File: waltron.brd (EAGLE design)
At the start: 53.6 x 45.1 mm, 25 parts, among them IC1 4049N, U1 LM386

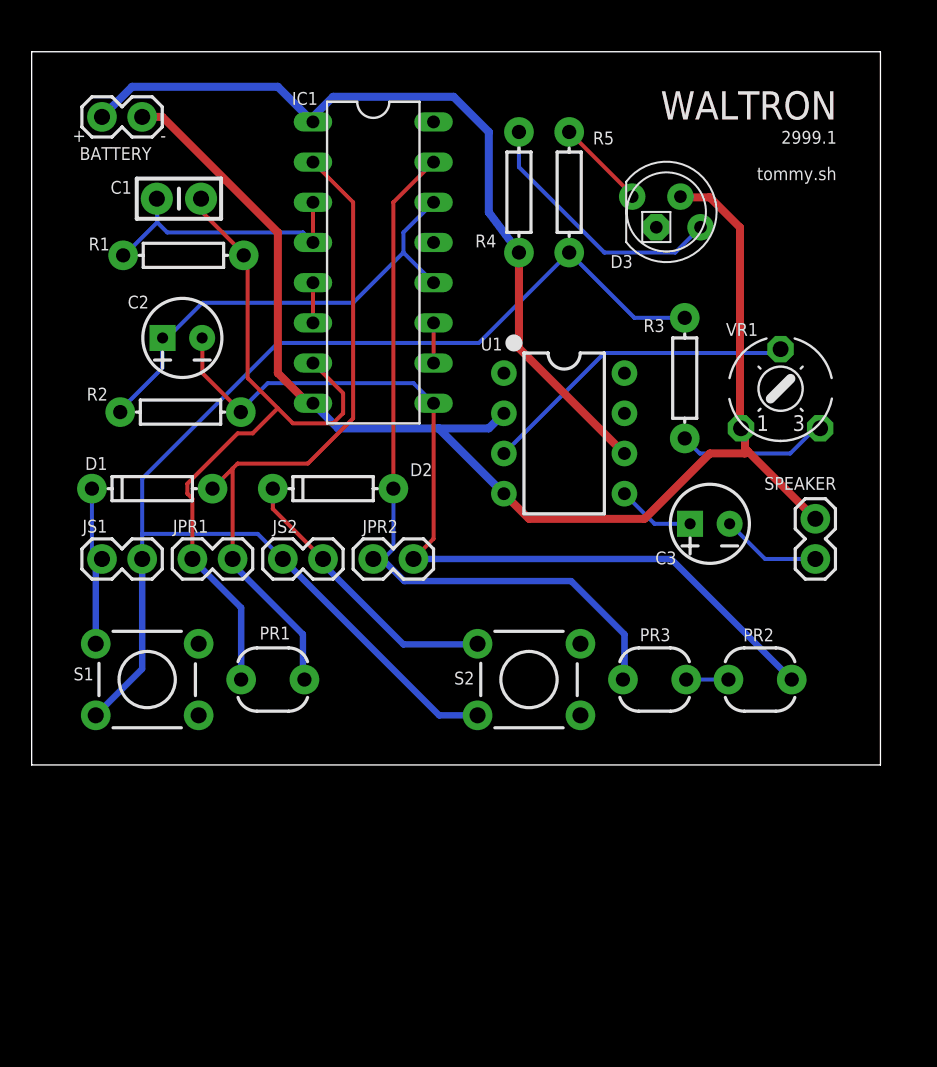
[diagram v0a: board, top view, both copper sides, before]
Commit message: Update schematic w/ 2999.1 concerns
- use IC name for LM386 instead of U1
- switch trim pot to model used in 4step
- add switch connection
- consistent J names for speaker and battery
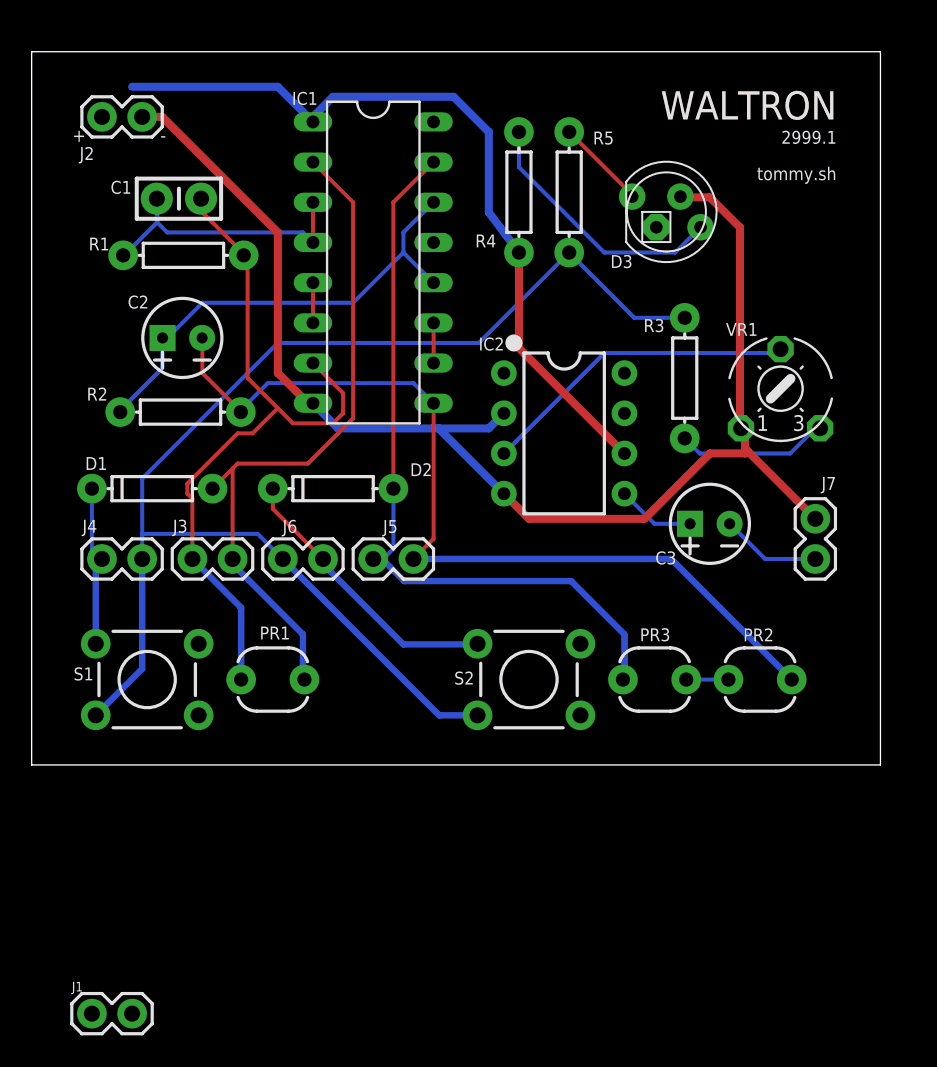
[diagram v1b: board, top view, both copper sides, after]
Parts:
- added J1: On Switch, SparkFun-Connectors:1X02
- J2: value 9v -> 9v battery
- J7: value 8ohm -> 8ohm speaker
- renumbered BATTERY to J2, JPR1 to J3, JPR2 to J5, JS1 to J4, JS2 to J6, SPEAKER to J7, U1 to IC2
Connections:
- new net N$19: J1.2, J2.1
- net V+: now also J1.1; no longer J2.1
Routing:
- net V+: track 51.6 -> 48.9 mm
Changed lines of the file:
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@@
 <attribute name="VALUE" x="31.4325" y="2.2225" size="0.6096" layer="27" font="vector" ratio="20" align="top-center"/>
 </element>
-<element name="U1" library="SparkFun-IC-Amplifiers" package="DIP08" value="LM386" x="33.655" y="20.955" smashed="yes" rot="R270">
+<element name="IC2" library="SparkFun-IC-Amplifiers" package="DIP08" value="LM386" x="33.655" y="20.955" smashed="yes" rot="R270">
 <attribute name="NAME" x="29.0631375" y="26.19375" size="0.8128" layer="25" font="vector" ratio="10" align="bottom-center"/>
 <attribute name="PROD_ID" value="IC-10899" x="33.655" y="20.955" size="1.778" layer="27" rot="R270" display="off"/>
 <attribute name="VALUE" x="33.654996875" y="23.6536125" size="0.8128" layer="27" font="vector" ratio="10" align="bottom-center"/>
 </element>
-<element name="BATTERY" library="SparkFun-Connectors" package="1X02" value="9v" x="4.445" y="40.9575" smashed="yes">
+<element name="J2" library="SparkFun-Connectors" package="1X02" value="9v battery" x="4.445" y="40.9575" smashed="yes">
 <attribute name="NAME" x="3.029021875" y="38.23300625" size="0.8128" layer="25" font="vector" ratio="10"/>
 </element>
-<element name="SPEAKER" library="SparkFun-Connectors" package="1X02" value="8ohm" x="49.53" y="13.0175" smashed="yes" rot="R90">
+<element name="J7" library="SparkFun-Connectors" package="1X02" value="8ohm speaker" x="49.53" y="13.0175" smashed="yes" rot="R90">
 <attribute name="NAME" x="50.85201875" y="18.20015" size="0.8128" layer="25" font="vector" ratio="10" rot="R180"/>
 </element>
@@
 <attribute name="NAME" x="45.90170625" y="27.92785" size="0.8128" layer="25" font="vector" ratio="10" rot="R180"/>
 </element>
-<element name="JPR1" library="SparkFun-Connectors" package="1X02" value="" x="10.16" y="13.0175" smashed="yes">
+<element name="J3" library="SparkFun-Connectors" package="1X02" value="" x="10.16" y="13.0175" smashed="yes">
 <attribute name="NAME" x="8.925678125" y="14.6828" size="0.8128" layer="25" font="vector" ratio="10"/>
 <attribute name="VALUE" x="8.89" y="10.9855" size="0.6096" layer="27" font="vector" ratio="20"/>
 </element>
-<element name="JS1" library="SparkFun-Connectors" package="1X02" value="" x="4.445" y="13.0175" smashed="yes">
+<element name="J4" library="SparkFun-Connectors" package="1X02" value="" x="4.445" y="13.0175" smashed="yes">
 <attribute name="NAME" x="3.210678125" y="14.6828" size="0.8128" layer="25" font="vector" ratio="10"/>
 <attribute name="VALUE" x="3.175" y="10.9855" size="0.6096" layer="27" font="vector" ratio="20"/>
 </element>
-<element name="JPR2" library="SparkFun-Connectors" package="1X02" value="" x="24.13" y="13.0175" smashed="yes" rot="R180">
+<element name="J5" library="SparkFun-Connectors" package="1X02" value="" x="24.13" y="13.0175" smashed="yes" rot="R180">
 <attribute name="NAME" x="23.141821875" y="15.4797" size="0.8128" layer="25" font="vector" ratio="10" rot="R180"/>
 <attribute name="VALUE" x="25.4" y="15.0495" size="0.6096" layer="27" font="vector" ratio="20" rot="R180"/>
 </element>
-<element name="JS2" library="SparkFun-Connectors" package="1X02" value="" x="18.415" y="13.0175" smashed="yes" rot="R180">
+<element name="J6" library="SparkFun-Connectors" package="1X02" value="" x="18.415" y="13.0175" smashed="yes" rot="R180">
 <attribute name="NAME" x="16.791821875" y="15.4797" size="0.8128" layer="25" font="vector" ratio="10" rot="R180"/>
 <attribute name="VALUE" x="19.685" y="15.0495" size="0.6096" layer="27" font="vector" ratio="20" rot="R180"/>
@@
 <attribute name="NAME" x="36.57574375" y="31.409234375" size="0.8128" layer="21" font="vector" ratio="10"/>
 </element>
+<element name="J1" library="SparkFun-Connectors" package="1X02" value="On Switch" x="3.81" y="-15.71625"/>
 </elements>
 <signals>
@@
 <contactref element="R1" pad="P$1"/>
 <contactref element="C1" pad="1"/>
-<contactref element="JPR1" pad="1"/>
+<contactref element="J3" pad="1"/>
 <wire x1="10.16" y1="13.0175" x2="13.24" y2="9.9375" width="0.4064" layer="16"/>
 <wire x1="13.24" y1="9.9375" x2="13.24" y2="5.3975" width="0.4064" layer="16"/>
@@
 <contactref element="IC1" pad="2"/>
 <contactref element="D1" pad="A"/>
-<contactref element="JPR1" pad="2"/>
+<contactref element="J3" pad="2"/>
 <wire x1="12.7" y1="13.0175" x2="12.7" y2="12.7" width="0.4064" layer="16"/>
 <wire x1="12.7" y1="12.7" x2="17.145" y2="8.255" width="0.4064" layer="16"/>
@@
 <contactref element="C2" pad="2"/>
 <contactref element="PR2" pad="1"/>
-<contactref element="JPR2" pad="1"/>
+<contactref element="J5" pad="1"/>
 <wire x1="24.13" y1="13.0175" x2="40.4175" y2="13.0175" width="0.4064" layer="16"/>
 <wire x1="40.4175" y1="13.0175" x2="48.0375" y2="5.3975" width="0.4064" layer="16"/>
@@
 <contactref element="PR3" pad="2"/>
 <contactref element="D2" pad="A"/>
-<contactref element="JPR2" pad="2"/>
+<contactref element="J5" pad="2"/>
 <wire x1="21.59" y1="13.0175" x2="22.1543375" y2="13.0175" width="0.4064" layer="16"/>
 <wire x1="22.1543375" y1="13.0175" x2="23.5513375" y2="11.6205" width="0.4064" layer="16"/>
@@
 <contactref element="R3" pad="P$1"/>
 <contactref element="R5" pad="P$1"/>
-<contactref element="JS1" pad="2"/>
-<contactref element="JS2" pad="2"/>
+<contactref element="J4" pad="2"/>
+<contactref element="J6" pad="2"/>
 <wire x1="15.875" y1="13.0175" x2="25.7556" y2="3.1369" width="0.4064" layer="16"/>
 <wire x1="25.7556" y1="3.1369" x2="28.1813" y2="3.1369" width="0.4064" layer="16"/>
@@
 </signal>
 <signal name="N$14">
-<contactref element="U1" pad="5"/>
+<contactref element="IC2" pad="5"/>
 <contactref element="C3" pad="1"/>
 <wire x1="39.37" y1="15.24" x2="37.465" y2="17.145" width="0.254" layer="16"/>
@@
 <signal name="N$15">
 <contactref element="C3" pad="2"/>
-<contactref element="SPEAKER" pad="1"/>
+<contactref element="J7" pad="1"/>
 <wire x1="46.355" y1="13.0175" x2="44.1325" y2="15.24" width="0.254" layer="16"/>
 <wire x1="49.53" y1="13.0175" x2="46.355" y2="13.0175" width="0.254" layer="16"/>
@@
 <contactref element="D1" pad="C"/>
 <contactref element="S1" pad="1"/>
-<contactref element="JS1" pad="1"/>
+<contactref element="J4" pad="1"/>
 <wire x1="4.445" y1="13.0175" x2="4.0513" y2="12.6238" width="0.4064" layer="16"/>
 <wire x1="4.0513" y1="12.6238" x2="4.0513" y2="7.6581" width="0.4064" layer="16"/>
@@
 <contactref element="D2" pad="C"/>
 <contactref element="S2" pad="1"/>
-<contactref element="JS2" pad="1"/>
+<contactref element="J6" pad="1"/>
 <wire x1="18.415" y1="13.0175" x2="18.415" y2="12.7" width="0.4064" layer="16"/>
 <wire x1="18.415" y1="12.7" x2="23.495" y2="7.62" width="0.4064" layer="16"/>
@@
 </signal>
 <signal name="V+" class="1">
-<contactref element="BATTERY" pad="1"/>
-<contactref element="U1" pad="6"/>
+<contactref element="IC2" pad="6"/>
 <contactref element="R4" pad="P$1"/>
 <contactref element="IC1" pad="1"/>
 <wire x1="15.5575" y1="42.8625" x2="17.78" y2="40.64" width="0.508" layer="16"/>
 <wire x1="6.35" y1="42.8625" x2="15.5575" y2="42.8625" width="0.508" layer="16"/>
-<wire x1="4.445" y1="40.9575" x2="6.35" y2="42.8625" width="0.508" layer="16"/>
 <wire x1="30.7975" y1="26.3525" x2="37.465" y2="19.685" width="0.508" layer="1"/>
 <wire x1="30.7975" y1="32.385" x2="30.7975" y2="26.3525" width="0.508" layer="1"/>
@@
 <wire x1="30.7975" y1="32.385" x2="28.8925" y2="34.925" width="0.508" layer="16"/>
 <wire x1="17.78" y1="40.64" x2="17.78" y2="40.9575" width="0.508" layer="16"/>
+<contactref element="J1" pad="1"/>
+<wire x1="3.81" y1="-15.71625" x2="37.465" y2="19.685" width="0" layer="19" extent="1-1"/>
 </signal>
 <signal name="GND" class="1">
-<contactref element="U1" pad="2"/>
-<contactref element="U1" pad="4"/>
-<contactref element="SPEAKER" pad="2"/>
-<contactref element="BATTERY" pad="2"/>
+<contactref element="IC2" pad="2"/>
+<contactref element="IC2" pad="4"/>
+<contactref element="J7" pad="2"/>
+<contactref element="J2" pad="2"/>
 <contactref element="IC1" pad="8"/>
 <contactref element="VR1" pad="A"/>
@@
 <signal name="N$16">
 <contactref element="VR1" pad="S"/>
-<contactref element="U1" pad="3"/>
+<contactref element="IC2" pad="3"/>
 <wire x1="36.195" y1="26.035" x2="29.845" y2="19.685" width="0.254" layer="16"/>
 <wire x1="47.3075" y1="26.035" x2="36.195" y2="26.035" width="0.254" layer="16"/>
@@
 <wire x1="40.67534375" y1="32.385" x2="42.273234375" y2="33.982890625" width="0.254" layer="16"/>
 </signal>
+<signal name="N$19" class="1">
+<contactref element="J2" pad="1"/>
+<contactref element="J1" pad="2"/>
+<wire x1="6.35" y1="-15.71625" x2="4.445" y2="40.9575" width="0" layer="19" extent="1-1"/>
+</signal>
 </signals>

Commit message: Rip up and lay out board
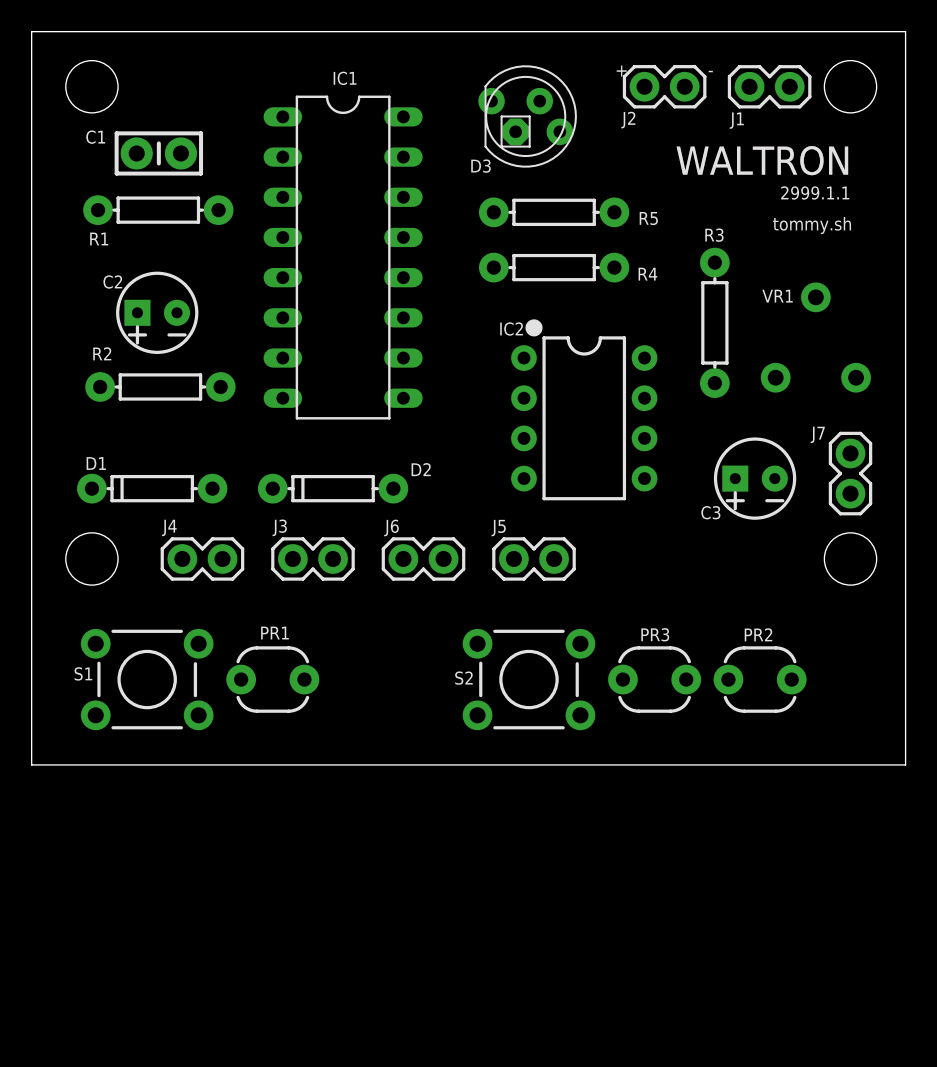
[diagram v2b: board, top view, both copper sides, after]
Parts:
- VR1: device adafruit:6MM -> SparkFun-Retired:TRIM_POT
- moved J1 71.8 mm to (45.4, 42.9)
- moved J2 34.3 mm to (38.7, 42.9)
- moved D3 10.7 mm to (31.2, 41.0)
- moved J5 8.89 mm to (33.0, 13.0)
- moved J6 7.62 mm to (26.0, 13.0)
- moved J3 6.35 mm to (16.5, 13.0)
- moved R4 5.26 mm to (33.0, 31.4), turned to 180 degrees
- moved J4 5.08 mm to (9.53, 13.0)
- moved J7 4.69 mm to (51.8, 17.1)
- moved C3 4.04 mm to (45.7, 18.1)
- moved R3 3.98 mm to (43.2, 27.9)
- moved R1 3.27 mm to (8.01, 35.1)
- moved C1 3.13 mm to (8.04, 38.6)
- moved VR1 2.34 mm to (49.6, 24.5), turned to 90 degrees
- moved C2 2.25 mm to (7.94, 28.6)
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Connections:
- net GND: now also VR1.3; no longer VR1.A
- net N$13: now also VR1.2; no longer VR1.E
- net N$16: now also VR1.1; no longer VR1.S
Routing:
- net GND: track 85.4 -> 0.00 mm
- net N$12: track 84.0 -> 0.00 mm
- net N$5: track 56.6 -> 0.00 mm
- net V+: track 48.9 -> 0.00 mm
- net N$8: track 47.8 -> 0.00 mm
- net N$3: track 45.5 -> 0.00 mm
- net N$4: track 43.2 -> 0.00 mm
- net N$7: track 29.9 -> 0.00 mm
- net N$16: track 20.3 -> 0.00 mm
- net N$11: track 18.0 -> 0.00 mm
- net N$2: track 17.4 -> 0.00 mm
- net N$18: track 17.0 -> 0.00 mm
- net N$9: track 10.6 -> 0.00 mm
- net N$13: track 9.61 -> 0.00 mm
- net N$15: track 6.34 -> 0.00 mm
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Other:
- board size 53.6 x 45.1 mm -> 55.2 x 46.3 mm
- board text added: "2999.1.1"
- board text removed: "2999.1"

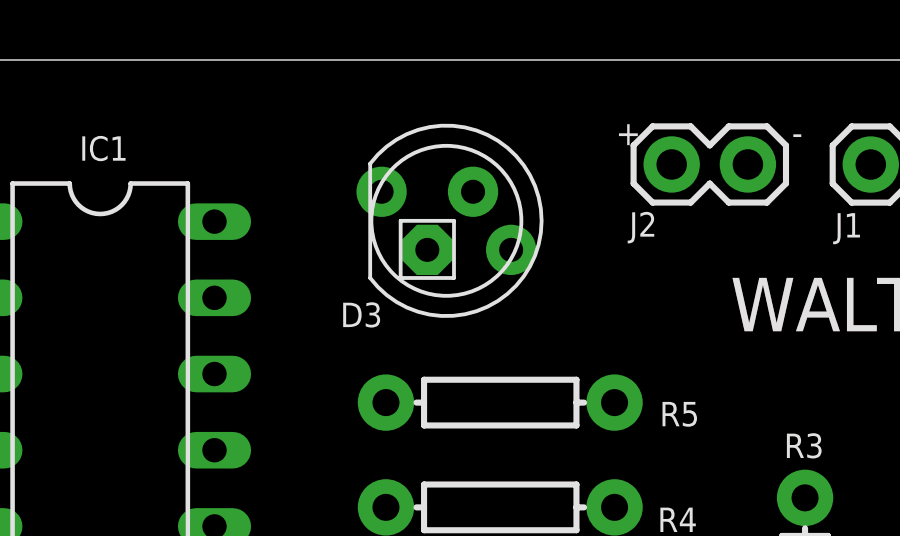
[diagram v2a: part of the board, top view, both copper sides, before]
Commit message: Add mounting holes and swap out LED for mirrored version
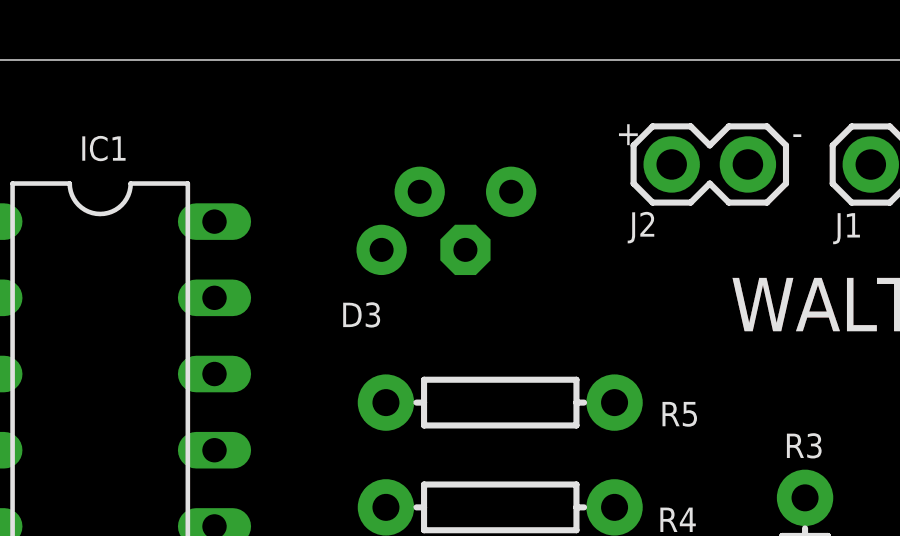
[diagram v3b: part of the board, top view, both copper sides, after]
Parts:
- D3: device adafruit:LED5MMRGB -> tommy:LED5MMRGB
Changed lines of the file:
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@@
 <attribute name="VALUE" x="27.305" y="15.0495" size="0.6096" layer="27" font="vector" ratio="20" rot="R180"/>
 </element>
-<element name="D3" library="adafruit" package="LED5MMRGB" value="5MMRGBLED" x="31.224234375" y="40.983790625" smashed="yes">
+<element name="D3" library="tommy" package="LED5MMRGB" value="5MMRGBLED" x="31.224234375" y="40.983790625" smashed="yes">
 <attribute name="NAME" x="27.68574375" y="37.441734375" size="0.8128" layer="21" font="vector" ratio="10"/>
 </element>
@@
 <wire x1="36.83" y1="34.925" x2="43.18" y2="31.75" width="0" layer="19" extent="1-1"/>
 <wire x1="23.495" y1="13.0175" x2="36.83" y2="34.925" width="0" layer="19" extent="1-1"/>
+<wire x1="28.1813" y1="3.1369" x2="23.495" y2="13.0175" width="0" layer="19" extent="1-1"/>
 <wire x1="12.065" y1="13.0175" x2="23.495" y2="13.0175" width="0" layer="19" extent="1-1"/>
-<wire x1="28.1813" y1="3.1369" x2="23.495" y2="13.0175" width="0" layer="19" extent="1-1"/>
 <wire x1="4.0513" y1="3.1369" x2="12.065" y2="13.0175" width="0" layer="19" extent="1-1"/>
 </signal>
@@
 <contactref element="S2" pad="1"/>
 <contactref element="J6" pad="1"/>
-<wire x1="26.035" y1="13.0175" x2="28.1813" y2="7.6581" width="0" layer="19" extent="1-1"/>
+<wire x1="28.1813" y1="7.6581" x2="26.035" y2="13.0175" width="0" layer="19" extent="1-1"/>
 <wire x1="15.24" y1="17.4625" x2="26.035" y2="13.0175" width="0" layer="19" extent="1-1"/>
 </signal>
@@
 <contactref element="R5" pad="P$2"/>
 <contactref element="D3" pad="1"/>
-<wire x1="29.21" y1="34.925" x2="29.065234375" y2="41.952190625" width="0" layer="19" extent="1-1"/>
+<wire x1="29.21" y1="34.925" x2="29.065234375" y2="40.015390625" width="0" layer="19" extent="1-1"/>
 </signal>
 <signal name="V+" class="1">
@@
 <contactref element="VR1" pad="3"/>
 <contactref element="D3" pad="3"/>
-<wire x1="32.113234375" y1="41.952190625" x2="41.275" y2="42.8625" width="0" layer="19" extent="1-1"/>
-<wire x1="31.115" y1="23.1775" x2="32.113234375" y2="41.952190625" width="0" layer="19" extent="1-1"/>
+<wire x1="31.859234375" y1="40.015390625" x2="41.275" y2="42.8625" width="0" layer="19" extent="1-1"/>
+<wire x1="31.115" y1="23.1775" x2="31.859234375" y2="40.015390625" width="0" layer="19" extent="1-1"/>
 <wire x1="31.115" y1="18.0975" x2="31.115" y2="23.1775" width="0" layer="19" extent="1-1"/>
 <wire x1="15.875" y1="23.1775" x2="31.115" y2="23.1775" width="0" layer="19" extent="1-1"/>
@@
 <contactref element="R4" pad="P$2"/>
 <contactref element="D3" pad="4"/>
-<wire x1="29.21" y1="31.4325" x2="33.383234375" y2="40.015390625" width="0" layer="19" extent="1-1"/>
+<wire x1="29.21" y1="31.4325" x2="33.383234375" y2="41.952190625" width="0" layer="19" extent="1-1"/>
 </signal>
 <signal name="N$19" class="1">
